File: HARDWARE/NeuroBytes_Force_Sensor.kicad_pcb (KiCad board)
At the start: 2 copper layers, 54 x 19 mm, 26 parts, among them P1 JST_GH_5-pos, P6 CONN_01X04, P7 CONN_01X04, Q1 MMBT3904, Q2 MMBT3904, Q3 MMBT3904, SW1 SW_PUSH, U1 STM32L011Gx, U2 3v3 LDO, U3 RClamp0503F

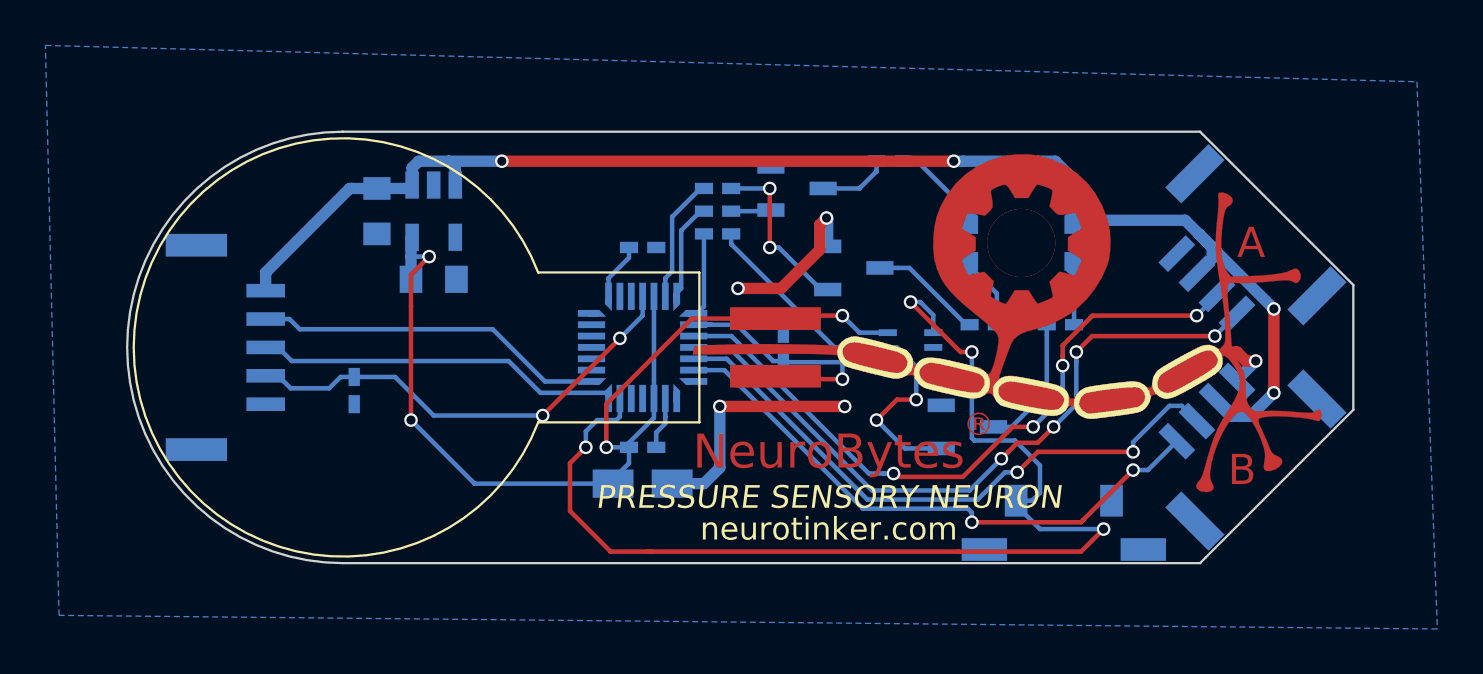
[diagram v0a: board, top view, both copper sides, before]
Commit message: updated footprints to include B.Fab outlines. minor routing changes. re-generated Gerbers. added placement pdf.
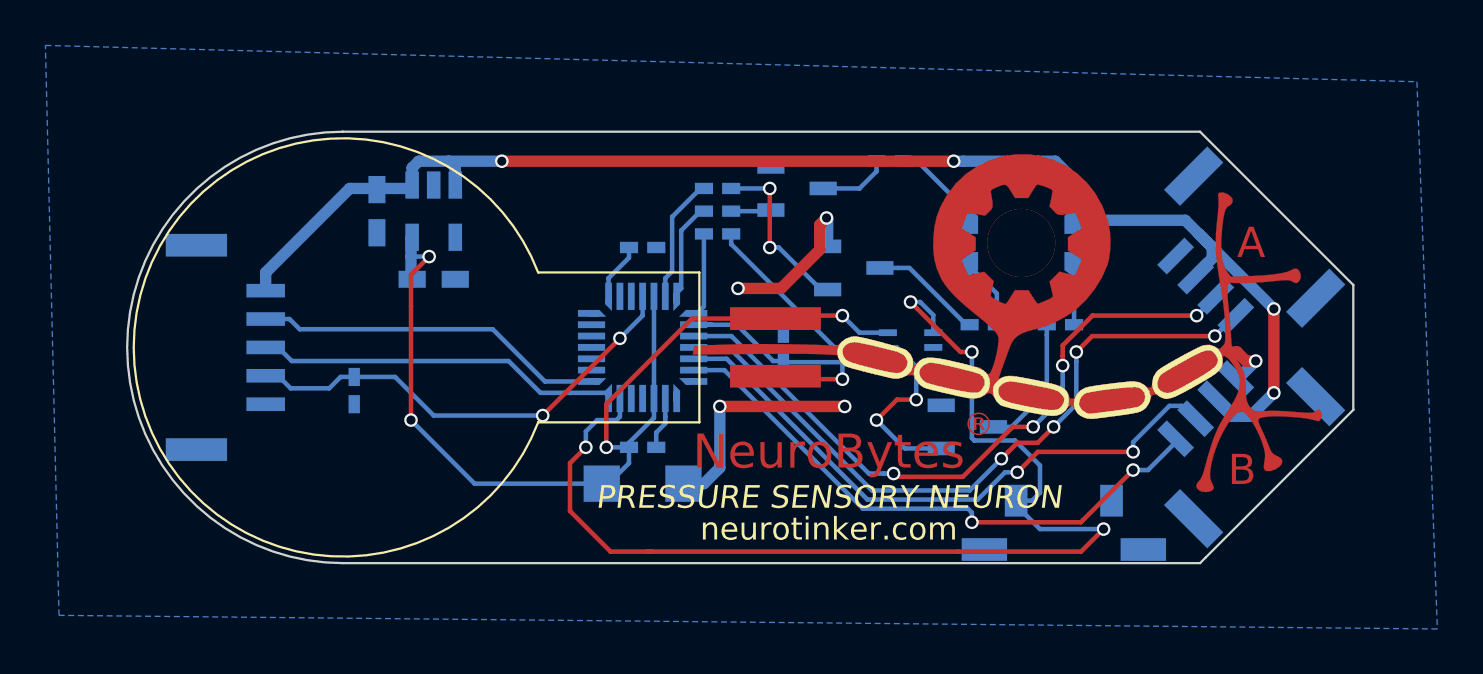
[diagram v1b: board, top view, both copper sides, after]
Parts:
- C1, C4: footprint KiCad_Footprints:ZF_SMD_NonPol_0603 -> Capacitors_SMD:C_0603_HandSoldering
- moved P6 0.81 mm to (139.2, 77.1)
- moved P7 0.81 mm to (139.2, 84.9)
